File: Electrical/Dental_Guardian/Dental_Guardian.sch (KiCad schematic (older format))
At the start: 25 parts

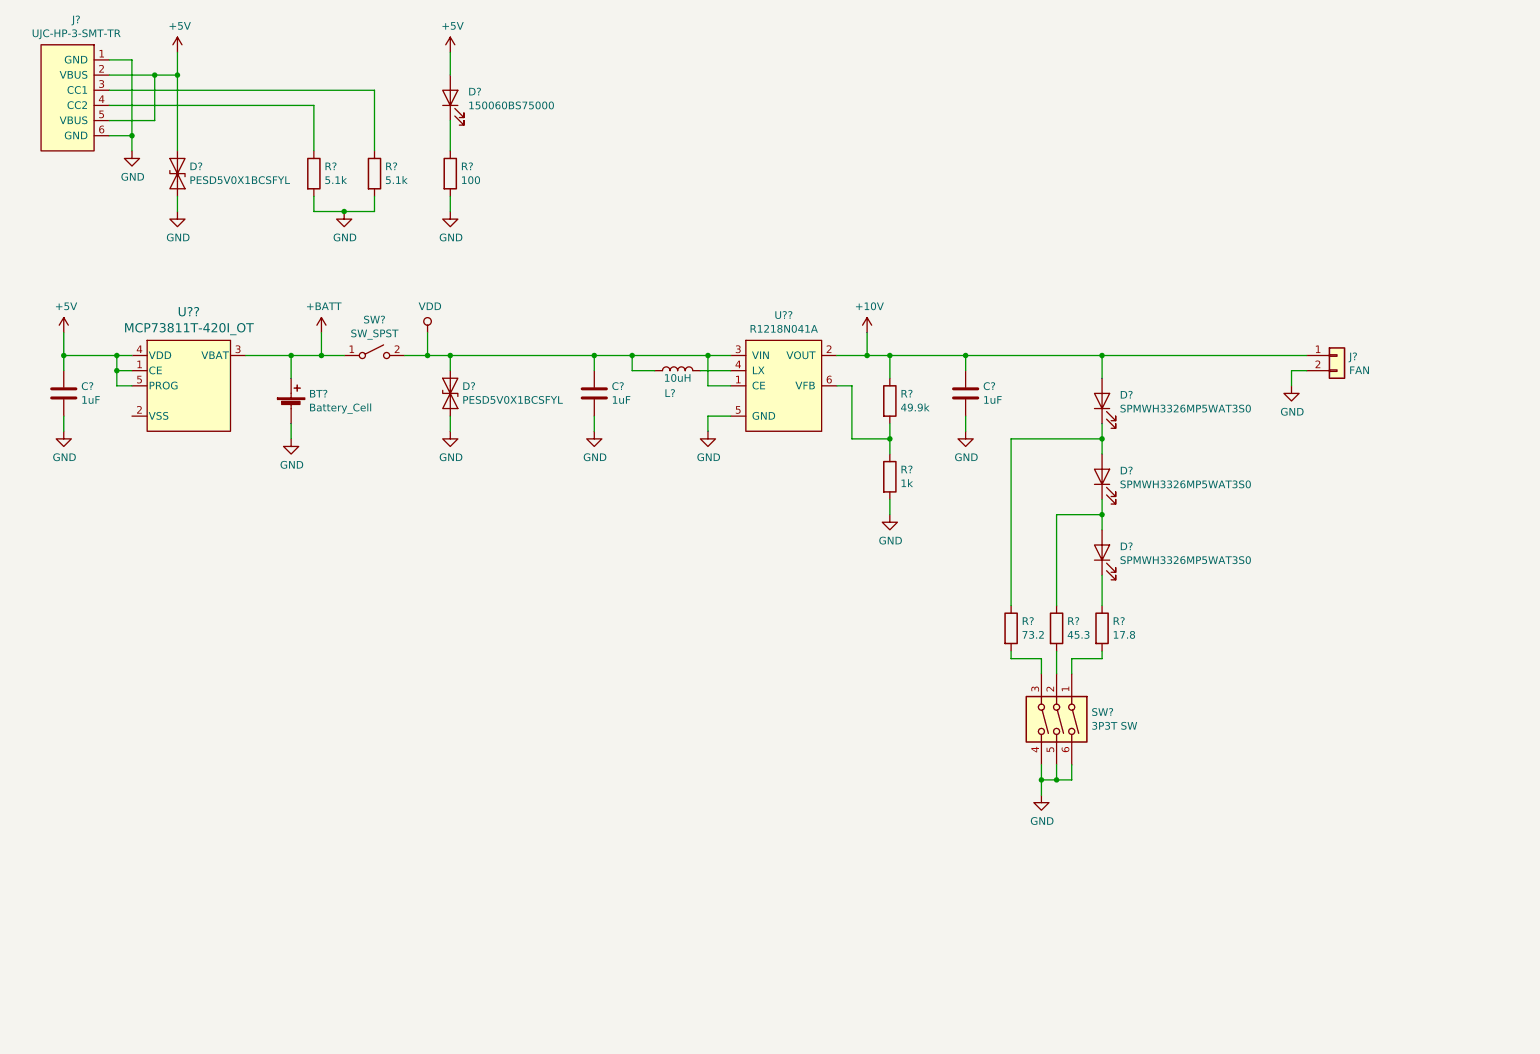
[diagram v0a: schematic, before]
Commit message: [Design] Replace Li battery circuit with AA batteries
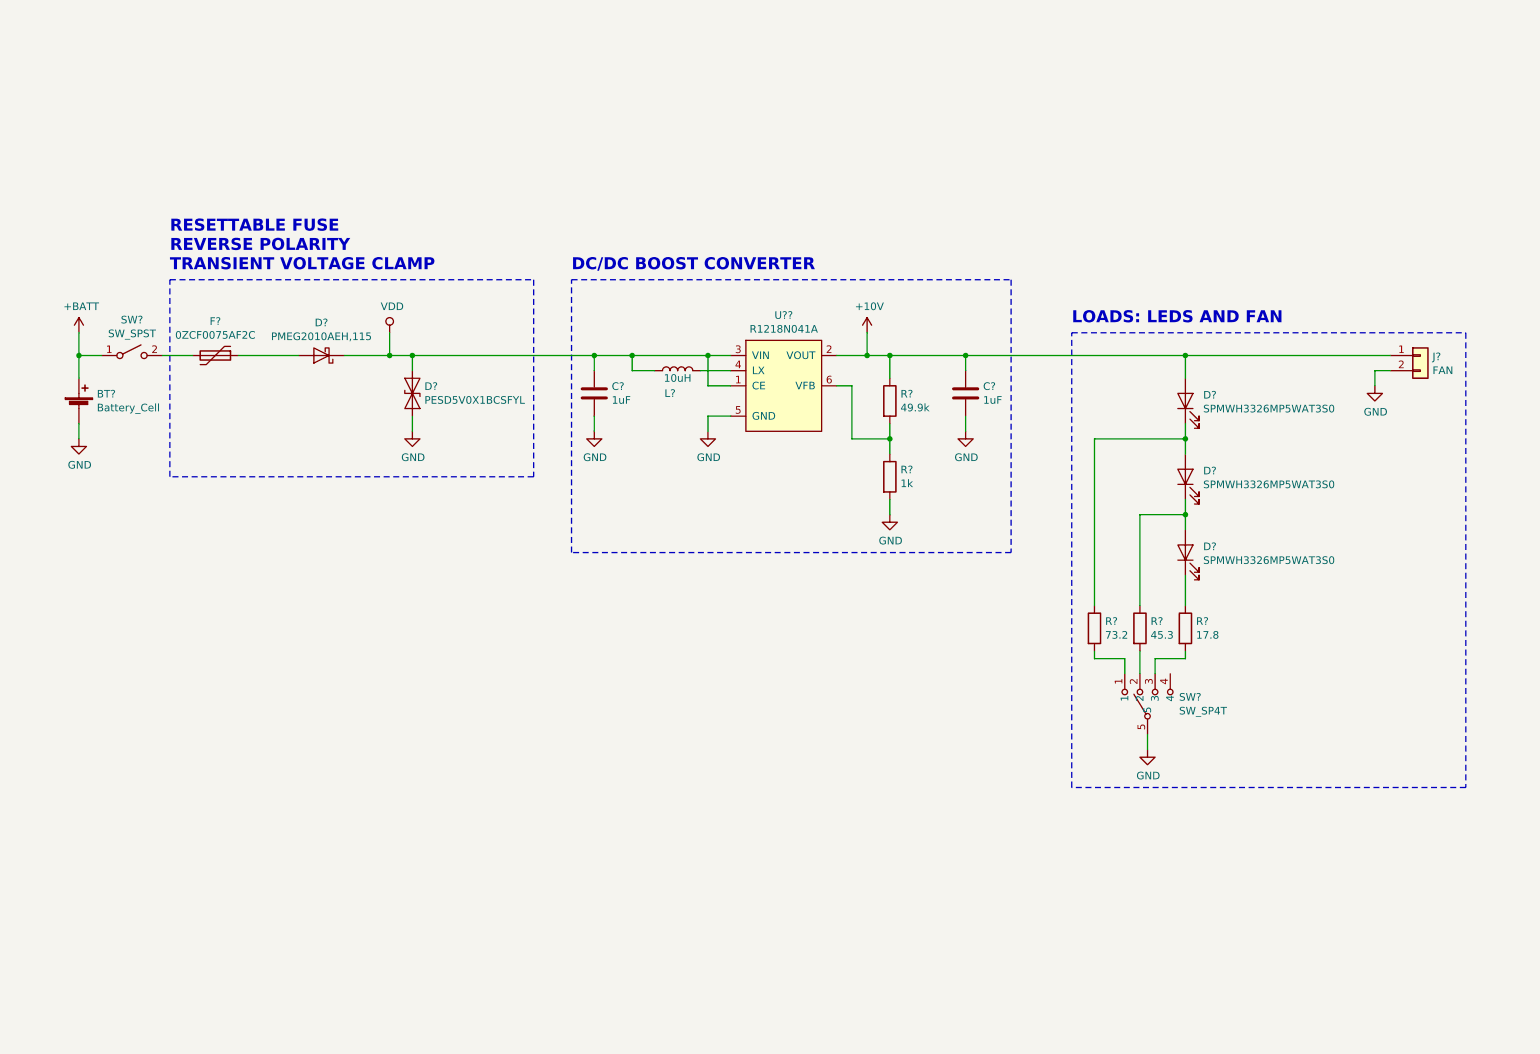
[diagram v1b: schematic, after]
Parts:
- removed C?: 1uF, symbol Device:C
- removed D?: PESD5V0X1BCSFYL, symbol Device:D_TVS
- removed D?: 150060BS75000, symbol Device:LED
- removed J?: UJC-HP-3-SMT-TR, symbol Dental_Guardian:UJC-HP-3-SMT-TR
- removed R? (x2): 5.1k, symbol Device:R
- removed R?: 100, symbol Device:R
- removed SW?: 3P3T SW, symbol Switch:SW_DIP_x03
- removed U??: MCP73811T-420I_OT, SOT-23-5_MC_MCH, symbol Dental_Guardian:MCP73811T-420I_OT
- added D?: PMEG2010AEH,115, symbol Device:D_Schottky
- added F?: 0ZCF0075AF2C, symbol Device:Polyfuse
- added SW?: SW_SP4T, symbol Dental_Guardian:SW_SP4T
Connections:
- net GND: now also SW?.5
- net VDD: now also D?.1 (K); no longer SW?.2 (B)
- net at R?.2: now also SW?.3
- net at R?.2: now also SW?.2
- net at R?.2: now also SW?.1
- new net: F?.2, SW?.2 (B)
- new net: D?.2 (A), F?.1
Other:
- note added: "DC/DC BOOST CONVERTER"
- note added: "LOADS: LEDS AND FAN"
- note added: "RESETTABLE FUSE\nREVERSE POLARITY\nTRANSIENT VOLTAGE CLAMP"
- moved on the sheet: BT?, D?, J?, R?, SW?

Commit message: [ELEC] Finalize schematic and generate PDF
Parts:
- BT?: symbol Device:Battery_Cell -> Dental_Guardian-rescue:Battery_Cell-Device
- C? (x2): symbol Device:C -> Dental_Guardian-rescue:C-Device
- D?: symbol Device:D_TVS -> Dental_Guardian-rescue:D_TVS-Device
- D? (x3): symbol Device:LED -> Dental_Guardian-rescue:LED-Device
- D?: symbol Device:D_Schottky -> Dental_Guardian-rescue:D_Schottky-Device
- F?: symbol Device:Polyfuse -> Dental_Guardian-rescue:Polyfuse-Device
- J?: symbol Connector_Generic:Conn_01x02 -> Dental_Guardian-rescue:Conn_01x02-Connector_Generic
- L?: symbol Device:L -> Dental_Guardian-rescue:L-Device
- R? (x5): symbol Device:R -> Dental_Guardian-rescue:R-Device
- SW?: symbol Switch:SW_SPST -> Dental_Guardian-rescue:SW_SPST-Switch
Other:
- note added: "2021-02-01"
- note added: "A"
- note added: "LEDs and Fan Driver"
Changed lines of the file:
@@
 $EndDescr
 $Comp
-L Device:Battery_Cell BT?
+L Dental_Guardian-rescue:Battery_Cell-Device BT?
 U 1 1 6019D20D
 P 1150 3500
@@
 $EndComp
 $Comp
-L Device:R R?
+L Dental_Guardian-rescue:R-Device R?
 U 1 1 6019F5CD
 P 6500 3450
@@
 $EndComp
 $Comp
-L Device:R R?
+L Dental_Guardian-rescue:R-Device R?
 U 1 1 601A089E
 P 6500 3950
@@
 	6500 3150 6350 3150
 $Comp
-L Device:L L?
+L Dental_Guardian-rescue:L-Device L?
 U 1 1 601A5B40
 P 5100 3250
@@
 	5300 3150 5450 3150
 $Comp
-L power:GND #PWR?
+L Dental_Guardian-rescue:GND-power #PWR?
 U 1 1 601A94DD
 P 5300 3650
@@
 	5300 3550 5450 3550
 $Comp
-L power:GND #PWR?
+L Dental_Guardian-rescue:GND-power #PWR?
 U 1 1 601AA227
 P 6500 4200
@@
 	6500 4100 6500 4200
 $Comp
-L Device:C C?
+L Dental_Guardian-rescue:C-Device C?
 U 1 1 601AC0C6
 P 4550 3400
@@
 	4550 3550 4550 3650
 $Comp
-L power:GND #PWR?
+L Dental_Guardian-rescue:GND-power #PWR?
 U 1 1 601AD94A
 P 4550 3650
@@
 $EndComp
 $Comp
-L Device:D_TVS D?
+L Dental_Guardian-rescue:D_TVS-Device D?
 U 1 1 601C06EE
 P 3350 3400
@@
 	3350 3650 3350 3550
 $Comp
-L power:GND #PWR?
+L Dental_Guardian-rescue:GND-power #PWR?
 U 1 1 601E46DE
 P 3350 3650
@@
 $EndComp
 $Comp
-L power:+BATT #PWR?
+L Dental_Guardian-rescue:+BATT-power #PWR?
 U 1 1 601EAA91
 P 1150 3000
@@
 	1150 3700 1150 3600
 $Comp
-L power:GND #PWR?
+L Dental_Guardian-rescue:GND-power #PWR?
 U 1 1 601EDBB1
 P 1150 3700
@@
 	3350 3150 3350 3250
 $Comp
-L Device:C C?
+L Dental_Guardian-rescue:C-Device C?
 U 1 1 601FD659
 P 7000 3400
@@
 	7000 3550 7000 3650
 $Comp
-L power:GND #PWR?
+L Dental_Guardian-rescue:GND-power #PWR?
 U 1 1 601FD661
 P 7000 3650
@@
 Connection ~ 6500 3150
 $Comp
-L power:+10V #PWR?
+L Dental_Guardian-rescue:+10V-power #PWR?
 U 1 1 601FFD52
 P 6350 3000
@@
 	6350 3000 6350 3150
 $Comp
-L Switch:SW_SPST SW?
+L Dental_Guardian-rescue:SW_SPST-Switch SW?
 U 1 1 6020947E
 P 1500 3150
@@
 	1300 3150 1150 3150
 $Comp
-L power:VDD #PWR?
+L Dental_Guardian-rescue:VDD-power #PWR?
 U 1 1 6024E2E9
 P 3200 3000
@@
 Connection ~ 3350 3150
 $Comp
-L Device:LED D?
+L Dental_Guardian-rescue:LED-Device D?
 U 1 1 60278D89
 P 8450 3450
@@
 $EndComp
 $Comp
-L Device:LED D?
+L Dental_Guardian-rescue:LED-Device D?
 U 1 1 60288065
 P 8450 3950
@@
 $EndComp
 $Comp
-L Device:LED D?
+L Dental_Guardian-rescue:LED-Device D?
 U 1 1 60289645
 P 8450 4450
@@
 $EndComp
 $Comp
-L Device:R R?
+L Dental_Guardian-rescue:R-Device R?
 U 1 1 602A59BD
 P 8450 4950
@@
 $EndComp
 $Comp
-L Device:R R?
+L Dental_Guardian-rescue:R-Device R?
 U 1 1 602A7555
 P 7850 4950
@@
 $EndComp
 $Comp
-L Device:R R?
+L Dental_Guardian-rescue:R-Device R?
 U 1 1 602A8BC8
 P 8150 4950
@@
 	7850 5100 7850 5150
 $Comp
-L power:GND #PWR?
+L Dental_Guardian-rescue:GND-power #PWR?
 U 1 1 602CDFB9
 P 8200 5750
@@
 	8200 5650 8200 5750
 $Comp
-L Connector_Generic:Conn_01x02 J?
+L Dental_Guardian-rescue:Conn_01x02-Connector_Generic J?
 U 1 1 602E9269
 P 10000 3150
@@
 $EndComp
 $Comp
-L power:GND #PWR?
+L Dental_Guardian-rescue:GND-power #PWR?
 U 1 1 602F0ABA
 P 9700 3350
@@
 	8450 3150 9800 3150
 $Comp
-L Device:D_Schottky D?
+L Dental_Guardian-rescue:D_Schottky-Device D?
 U 1 1 6033A248
 P 2750 3150
@@
 $EndComp
 $Comp
-L Device:Polyfuse F?
+L Dental_Guardian-rescue:Polyfuse-Device F?
 U 1 1 6033BF61
 P 2050 3150
@@
 Text Notes 7700 2950 0    79   ~ 16
 LOADS: LEDS AND FAN
+Text Notes 7400 7500 0    79   ~ 0
+LEDs and Fan Driver
+Text Notes 10600 7650 0    79   ~ 0
+A
+Text Notes 8150 7650 0    79   ~ 0
+2021-02-01
 $EndSCHEMATC
